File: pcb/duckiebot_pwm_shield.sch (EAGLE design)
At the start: 10 parts, among them J1 RASPBERRYPI-40-PIN-GPIO

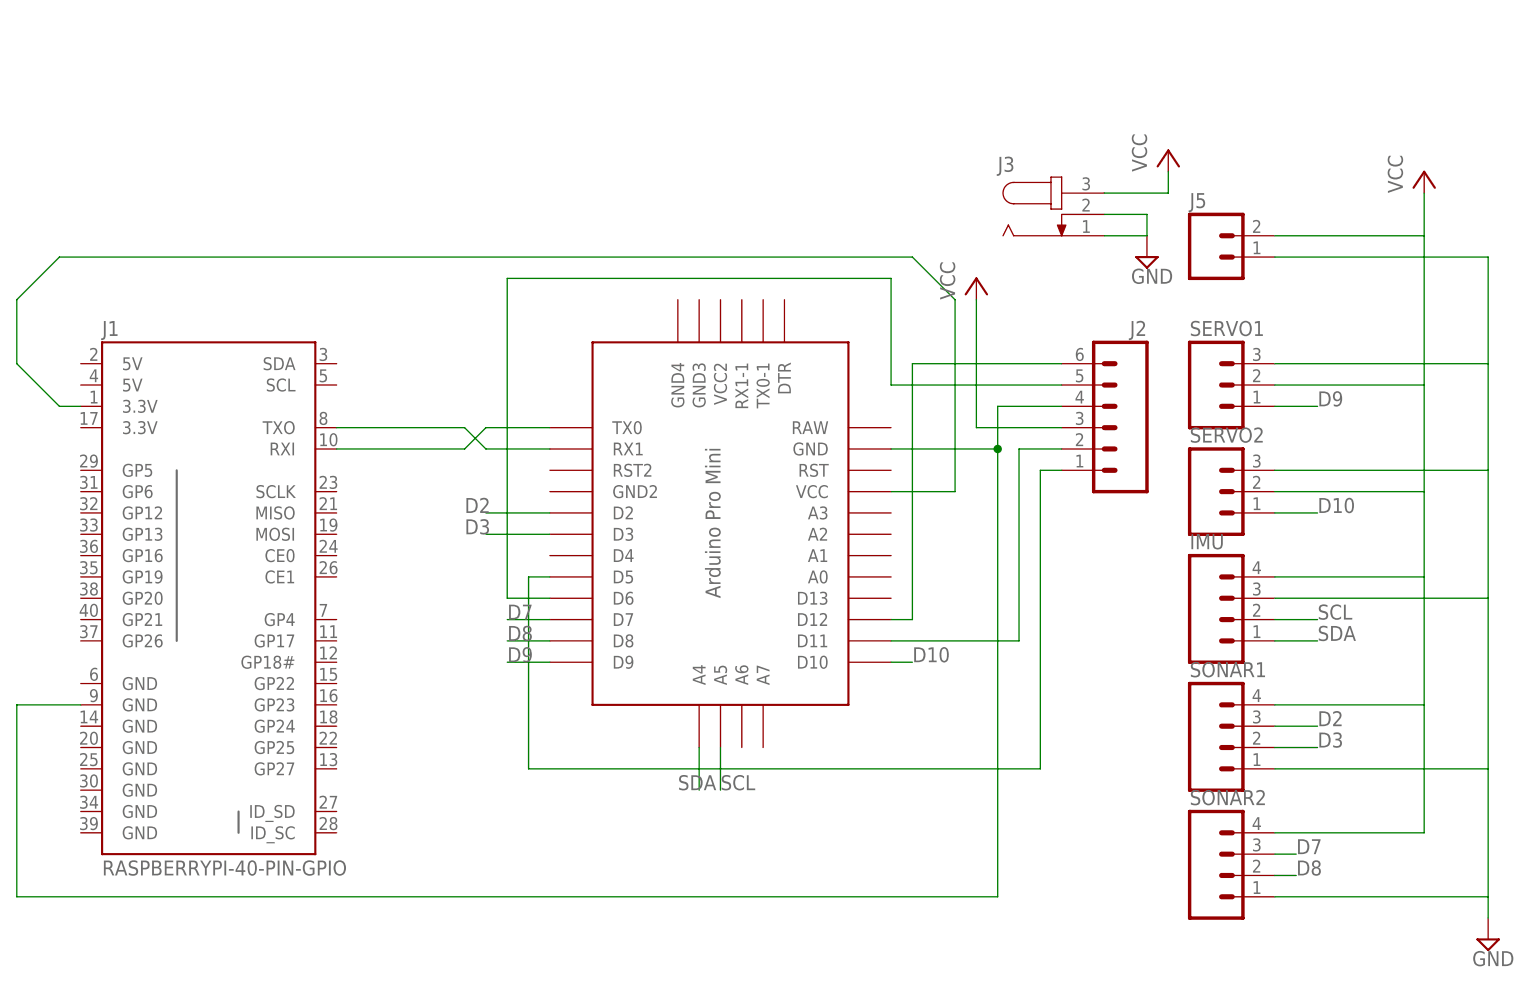
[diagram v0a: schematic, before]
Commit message: duckiebot shield updated v1.1
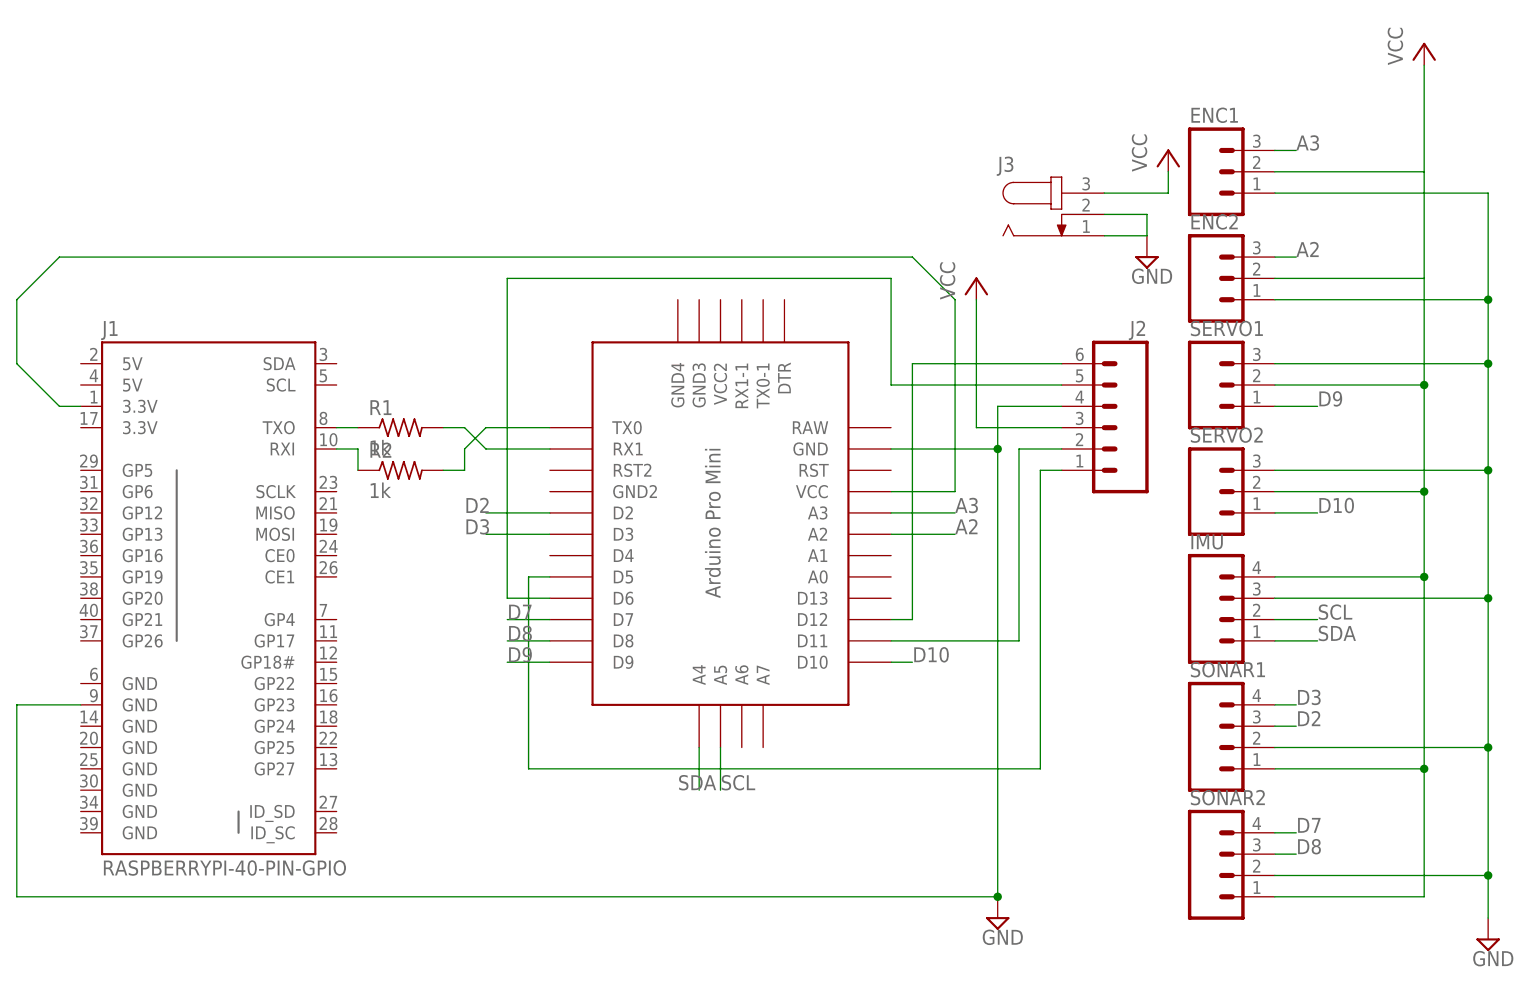
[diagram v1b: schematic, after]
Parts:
- removed J5: (no value), SparkFun-Connectors:M02PTH3
- added ENC1, ENC2: (no value), SparkFun-Connectors:M03LONGPADS
- added R1, R2: 1k, adafruit:R-US_0204/5
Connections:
- new net A2: ENC2.3, U$2.A2
- new net A3: ENC1.3, U$2.A3
- new net N$3: J1.RXI, R2.1
- new net N$4: J1.TXO, R1.1
- net D3: now also SONAR1.4; no longer SONAR1.2
- net D7: now also SONAR2.4; no longer SONAR2.3
- net D8: now also SONAR2.3; no longer SONAR2.2
- net GND: now also ENC1.1, ENC2.1, SONAR1.2, SONAR2.2; no longer J5.1, SONAR1.1, SONAR2.1
- net N$1: now also R1.2; no longer J1.TXO
- net N$2: now also R2.2; no longer J1.RXI
- net VCC: now also ENC1.2, ENC2.2, SONAR1.1, SONAR2.1; no longer J5.2, SONAR1.4, SONAR2.4

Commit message: duckiebot shield v1.2, duck missing :(
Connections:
- net N$5 renamed 3.3V
- removed net A2: ENC2.3, U$2.A2
- removed net A3: ENC1.3, U$2.A3
- new net D13: SONAR1.4, U$2.D13
- new net D4: SONAR1.3, U$2.D4
- net D2: now also ENC1.3; no longer SONAR1.3
- net D3: now also ENC2.3; no longer SONAR1.4
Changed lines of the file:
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@@
 </segment>
 </net>
-<net name="N$5" class="0">
+<net name="3.3V" class="0">
 <segment>
 <pinref part="J1" gate="G$1" pin="3.3V@1"/>
@@
 </segment>
 <segment>
-<pinref part="SONAR1" gate="G$1" pin="3"/>
-<wire x1="172.72" y1="22.86" x2="175.26" y2="22.86" width="0.1524" layer="91"/>
-<label x="175.26" y="22.86" size="1.778" layer="95"/>
+<pinref part="ENC1" gate="J$1" pin="3"/>
+<wire x1="172.72" y1="91.44" x2="175.26" y2="91.44" width="0.1524" layer="91"/>
 </segment>
 </net>
@@
 </segment>
 <segment>
-<pinref part="SONAR1" gate="G$1" pin="4"/>
-<wire x1="172.72" y1="25.4" x2="175.26" y2="25.4" width="0.1524" layer="91"/>
-<label x="175.26" y="25.4" size="1.778" layer="95"/>
+<pinref part="ENC2" gate="J$1" pin="3"/>
+<wire x1="172.72" y1="78.74" x2="175.26" y2="78.74" width="0.1524" layer="91"/>
 </segment>
 </net>
@@
 <wire x1="172.72" y1="48.26" x2="177.8" y2="48.26" width="0.1524" layer="91"/>
 <label x="177.8" y="48.26" size="1.778" layer="95"/>
-</segment>
-</net>
-<net name="A3" class="0">
-<segment>
-<pinref part="U$2" gate="G$1" pin="A3"/>
-<wire x1="127" y1="48.26" x2="134.62" y2="48.26" width="0.1524" layer="91"/>
-<label x="134.62" y="48.26" size="1.778" layer="95"/>
-</segment>
-<segment>
-<pinref part="ENC1" gate="J$1" pin="3"/>
-<wire x1="172.72" y1="91.44" x2="175.26" y2="91.44" width="0.1524" layer="91"/>
-<label x="175.26" y="91.44" size="1.778" layer="95"/>
-</segment>
-</net>
-<net name="A2" class="0">
-<segment>
-<pinref part="U$2" gate="G$1" pin="A2"/>
-<wire x1="127" y1="45.72" x2="134.62" y2="45.72" width="0.1524" layer="91"/>
-<label x="134.62" y="45.72" size="1.778" layer="95"/>
-</segment>
-<segment>
-<pinref part="ENC2" gate="J$1" pin="3"/>
-<wire x1="172.72" y1="78.74" x2="175.26" y2="78.74" width="0.1524" layer="91"/>
-<label x="175.26" y="78.74" size="1.778" layer="95"/>
 </segment>
 </net>
@@
 </segment>
 </net>
+<net name="D13" class="0">
+<segment>
+<pinref part="U$2" gate="G$1" pin="D13"/>
+<wire x1="127" y1="38.1" x2="132.08" y2="38.1" width="0.1524" layer="91"/>
+<label x="132.08" y="38.1" size="1.778" layer="95"/>
+</segment>
+<segment>
+<pinref part="SONAR1" gate="G$1" pin="4"/>
+<wire x1="172.72" y1="25.4" x2="177.8" y2="25.4" width="0.1524" layer="91"/>
+</segment>
+</net>
+<net name="D4" class="0">
+<segment>
+<pinref part="U$2" gate="G$1" pin="D4"/>
+<wire x1="86.36" y1="43.18" x2="83.82" y2="43.18" width="0.1524" layer="91"/>
+<label x="83.82" y="43.18" size="1.778" layer="95"/>
+</segment>
+<segment>
+<pinref part="SONAR1" gate="G$1" pin="3"/>
+<wire x1="172.72" y1="22.86" x2="175.26" y2="22.86" width="0.1524" layer="91"/>
+</segment>
+</net>

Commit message: v1.3, falta arreglar el layer del pato ql
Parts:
- renumbered J2 to H-BRIDGE, J3 to PWR
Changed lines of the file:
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@@
 <parts>
 <part name="J1" library="SparkFun-Boards" deviceset="RASPBERRYPI-40-PIN-GPIO" device=""/>
-<part name="J2" library="SparkFun-Connectors" deviceset="M06" device="LONGPADS"/>
+<part name="H-BRIDGE" library="SparkFun-Connectors" deviceset="M06" device="LONGPADS"/>
 <part name="P+1" library="supply1" deviceset="VCC" device=""/>
 <part name="U$2" library="Arduino-clone" deviceset="PRO-MINI" device=""/>
-<part name="J3" library="con-jack" deviceset="JACK-PLUG" device="0"/>
+<part name="PWR" library="con-jack" deviceset="JACK-PLUG" device="0"/>
 <part name="P+2" library="supply1" deviceset="VCC" device=""/>
 <part name="SUPPLY1" library="supply2" deviceset="GND" device=""/>
@@
 <instances>
 <instance part="J1" gate="G$1" x="45.72" y="40.64"/>
-<instance part="J2" gate="G$1" x="152.4" y="58.42" rot="MR0"/>
+<instance part="H-BRIDGE" gate="G$1" x="152.4" y="58.42" rot="MR0"/>
 <instance part="P+1" gate="VCC" x="137.16" y="76.2"/>
 <instance part="U$2" gate="G$1" x="109.22" y="38.1"/>
-<instance part="J3" gate="G$1" x="147.32" y="83.82"/>
+<instance part="PWR" gate="G$1" x="147.32" y="83.82"/>
 <instance part="P+2" gate="VCC" x="160.02" y="91.44"/>
 <instance part="SUPPLY1" gate="GND" x="157.48" y="78.74"/>
@@
 <pinref part="P+1" gate="VCC" pin="VCC"/>
 <wire x1="137.16" y1="73.66" x2="137.16" y2="58.42" width="0.1524" layer="91"/>
-<pinref part="J2" gate="G$1" pin="3"/>
+<pinref part="H-BRIDGE" gate="G$1" pin="3"/>
 <wire x1="137.16" y1="58.42" x2="147.32" y2="58.42" width="0.1524" layer="91"/>
 </segment>
 <segment>
 <pinref part="P+2" gate="VCC" pin="VCC"/>
-<pinref part="J3" gate="G$1" pin="3"/>
+<pinref part="PWR" gate="G$1" pin="3"/>
 <wire x1="160.02" y1="88.9" x2="160.02" y2="86.36" width="0.1524" layer="91"/>
 <wire x1="160.02" y1="86.36" x2="152.4" y2="86.36" width="0.1524" layer="91"/>
@@
 <pinref part="U$2" gate="G$1" pin="D12"/>
 <wire x1="129.54" y1="35.56" x2="127" y2="35.56" width="0.1524" layer="91"/>
-<pinref part="J2" gate="G$1" pin="6"/>
+<pinref part="H-BRIDGE" gate="G$1" pin="6"/>
 <wire x1="147.32" y1="66.04" x2="129.54" y2="66.04" width="0.1524" layer="91"/>
 </segment>
@@
 <pinref part="U$2" gate="G$1" pin="D6"/>
 <wire x1="81.28" y1="38.1" x2="86.36" y2="38.1" width="0.1524" layer="91"/>
-<pinref part="J2" gate="G$1" pin="5"/>
+<pinref part="H-BRIDGE" gate="G$1" pin="5"/>
 <wire x1="147.32" y1="63.5" x2="127" y2="63.5" width="0.1524" layer="91"/>
 </segment>
@@
 <wire x1="83.82" y1="17.78" x2="144.78" y2="17.78" width="0.1524" layer="91"/>
 <wire x1="144.78" y1="17.78" x2="144.78" y2="53.34" width="0.1524" layer="91"/>
-<pinref part="J2" gate="G$1" pin="1"/>
+<pinref part="H-BRIDGE" gate="G$1" pin="1"/>
 <wire x1="144.78" y1="53.34" x2="147.32" y2="53.34" width="0.1524" layer="91"/>
 </segment>
@@
 <pinref part="U$2" gate="G$1" pin="D11"/>
 <wire x1="142.24" y1="33.02" x2="127" y2="33.02" width="0.1524" layer="91"/>
-<pinref part="J2" gate="G$1" pin="2"/>
+<pinref part="H-BRIDGE" gate="G$1" pin="2"/>
 <wire x1="142.24" y1="55.88" x2="147.32" y2="55.88" width="0.1524" layer="91"/>
 </segment>
@@
 <segment>
 <pinref part="SUPPLY1" gate="GND" pin="GND"/>
-<pinref part="J3" gate="G$1" pin="1"/>
+<pinref part="PWR" gate="G$1" pin="1"/>
 <wire x1="157.48" y1="81.28" x2="152.4" y2="81.28" width="0.1524" layer="91"/>
-<pinref part="J3" gate="G$1" pin="2"/>
+<pinref part="PWR" gate="G$1" pin="2"/>
 <wire x1="152.4" y1="83.82" x2="157.48" y2="83.82" width="0.1524" layer="91"/>
 <wire x1="157.48" y1="83.82" x2="157.48" y2="81.28" width="0.1524" layer="91"/>
@@
 <wire x1="139.7" y1="2.54" x2="139.7" y2="55.88" width="0.1524" layer="91"/>
 <junction x="139.7" y="55.88"/>
-<pinref part="J2" gate="G$1" pin="4"/>
+<pinref part="H-BRIDGE" gate="G$1" pin="4"/>
 <wire x1="147.32" y1="60.96" x2="139.7" y2="60.96" width="0.1524" layer="91"/>
 <pinref part="SUPPLY3" gate="GND" pin="GND"/>

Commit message: fixed resistor size, v1.4 ready to build
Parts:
- R1, R2: device adafruit:R-US_0204/5 -> resistor:R-US_0309/10
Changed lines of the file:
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@@
 <?xml version="1.0" encoding="utf-8"?>
 <!DOCTYPE eagle SYSTEM "eagle.dtd">
-<eagle version="7.7.0">
+<eagle version="7.6.0">
 <drawing>
 <settings>
@@
 <part name="ENC2" library="SparkFun-Connectors" deviceset="M03" device="LONGPADS"/>
 <part name="SUPPLY3" library="supply2" deviceset="GND" device=""/>
-<part name="R1" library="adafruit" deviceset="R-US_" device="0204/5" value="1k"/>
-<part name="R2" library="adafruit" deviceset="R-US_" device="0204/5" value="1k"/>
+<part name="R1" library="resistor" deviceset="R-US_" device="0309/10" value="1k"/>
+<part name="R2" library="resistor" deviceset="R-US_" device="0309/10" value="1k"/>
 </parts>
 <sheets>
